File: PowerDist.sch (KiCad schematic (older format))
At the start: 14 parts, among them J5 CarPowerConnector, U6 PDS1-S12-S5, U7 NCP1117-3.3_SOT223

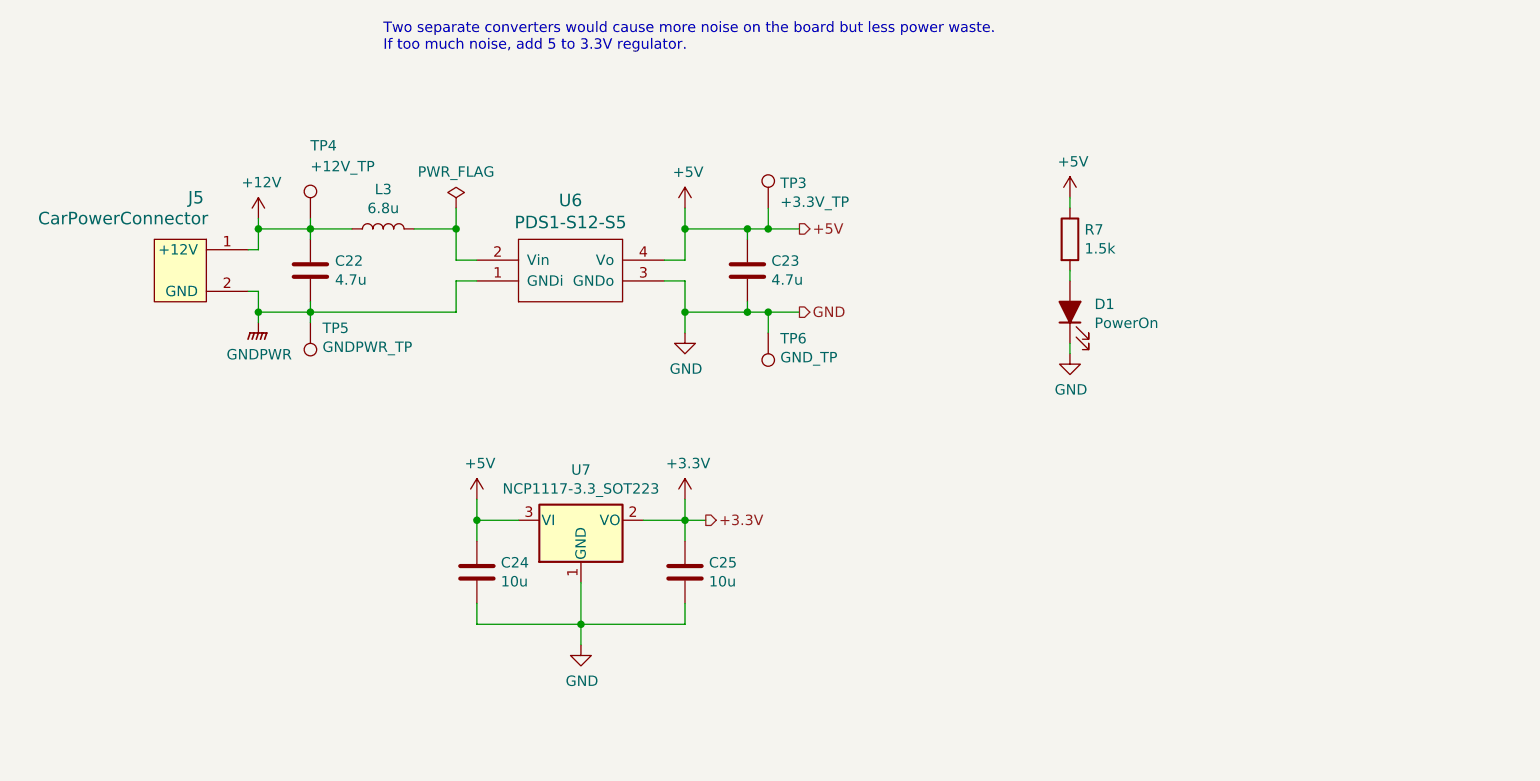
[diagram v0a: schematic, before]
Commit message: Adds LED for supplementals, deletes unncessary files, and links all symbols to the submodule
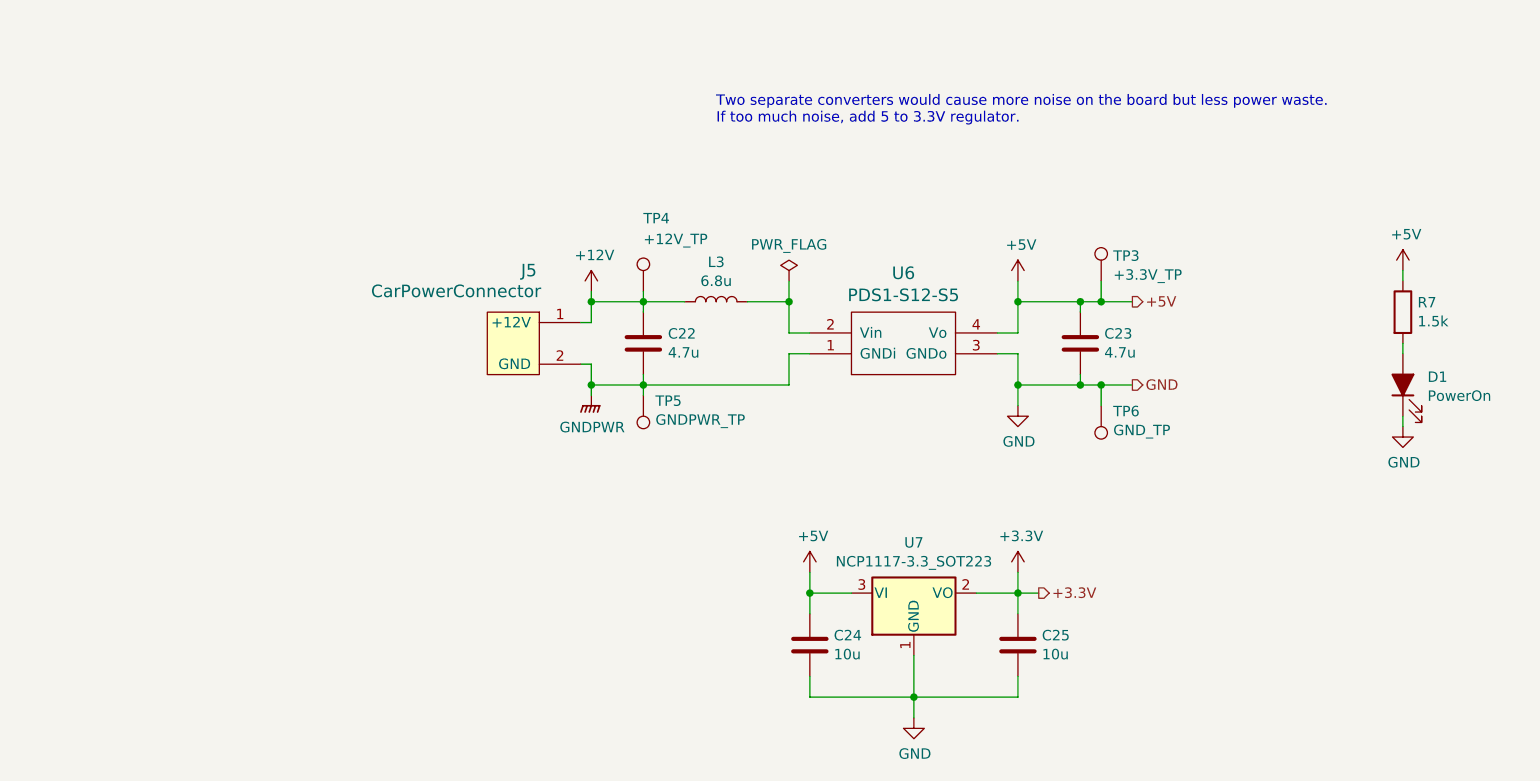
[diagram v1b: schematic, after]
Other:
- moved on the sheet: C22, C23, C24, C25, D1, J5, L3, R7, TP3, TP4, TP5, TP6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
